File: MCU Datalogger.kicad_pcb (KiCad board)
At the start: 2 copper layers, 29 parts, among them J1 Conn_01x04_Pin, J2 Conn_01x04_Pin, J3 Conn_01x09_Pin, J4 Conn_02x03_Odd_Even, U1 24LC1025, U2 24LC1025, U3 DS1337S_, U4 ATMEGA328P-AU, Y1 32.768 KHZ, Y2 16 MHz

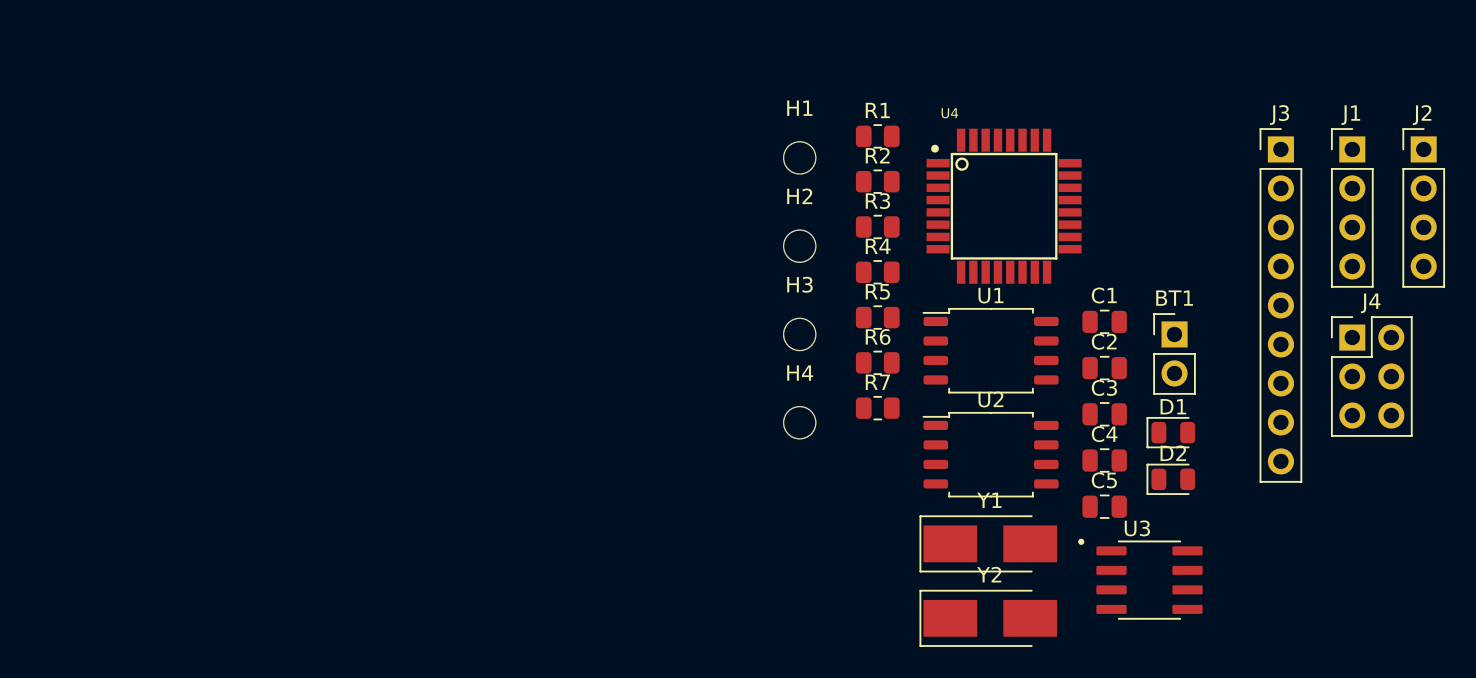
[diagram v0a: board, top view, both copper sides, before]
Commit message: Completed placement of footprints.
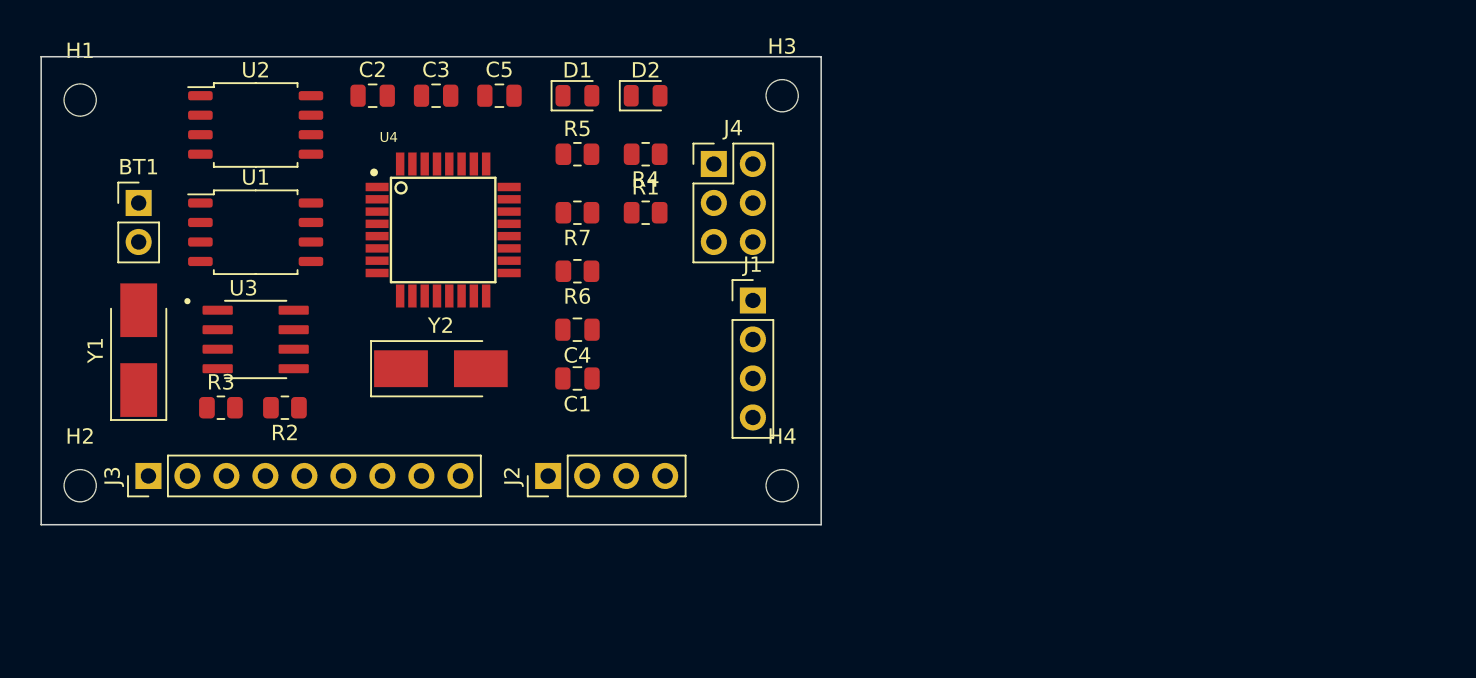
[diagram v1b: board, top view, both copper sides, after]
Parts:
- moved J3 76.8 mm to (83.2, 103.5), turned to 90 degrees
- moved BT1 68.0 mm to (82.5, 85.7)
- moved J2 60.9 mm to (109.2, 103.5), turned to 90 degrees
- moved U3 60.3 mm to (90.2, 94.6)
- moved Y1 56.9 mm to (82.5, 95.3), turned to 90 degrees
- moved U2 52.5 mm to (90.2, 80.6)
- moved C2 50.9 mm to (97.8, 78.7)
- moved H2 49.4 mm to (78.7, 104.1)
- moved U1 48.5 mm to (90.2, 87.6)
- moved C3 48.2 mm to (101.9, 78.7)
- moved C5 47.6 mm to (106.0, 78.7)
- moved H1 47.0 mm to (78.7, 79.0)
- moved D1 44.6 mm to (111.1, 78.7)
- moved R3 44.4 mm to (87.9, 99.1)
- moved J4 43.1 mm to (120.0, 83.2)
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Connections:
- Y1 pad 1: Net-(U3-X1) -> Net-(U3-X2)
- Y1 pad 2: Net-(U3-X2) -> Net-(U3-X1)
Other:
- board outline added: 50.8 x 30.5 mm

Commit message: Routing without GND VCC completed.
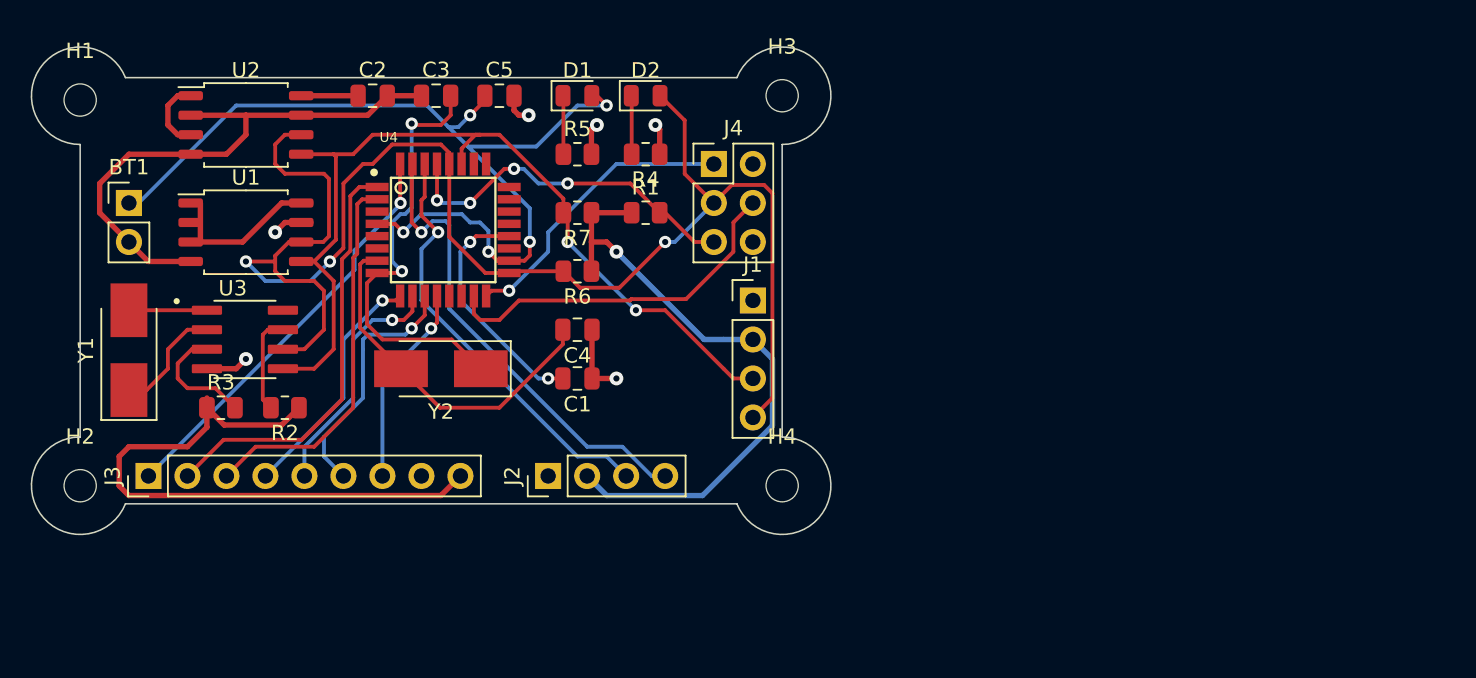
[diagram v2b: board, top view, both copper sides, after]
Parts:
- moved U3 0.70 mm to (89.5, 94.6)
- moved U1 0.64 mm to (89.5, 87.6)
- moved U2 0.64 mm to (89.5, 80.6)
- moved BT1 0.63 mm to (81.9, 85.7)
- moved Y1 0.63 mm to (81.9, 95.3)
- turned Y2 to 180 degrees
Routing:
- net /SCK: track 0.00 -> 102.3 mm, vias 0 -> 3
- net /Vcc: track 0.00 -> 101.9 mm, vias 0 -> 1
- net Net-(BT1-+): track 0.00 -> 61.5 mm, vias 0 -> 5
- net /SDA: track 0.00 -> 56.9 mm, vias 0 -> 2
- net GND: track 0.00 -> 52.4 mm, vias 0 -> 6
- net /TX: track 0.00 -> 31.0 mm, vias 0 -> 1
- net Net-(U4-PB7): track 0.00 -> 28.6 mm, vias 0 -> 2
- net /RX: track 0.00 -> 28.0 mm, vias 0 -> 1
- net /D3: track 0.00 -> 27.6 mm
- net /D2: track 0.00 -> 27.1 mm, vias 0 -> 1
- net /D4: track 0.00 -> 24.9 mm
- net /MOSI: track 0.00 -> 23.8 mm
- net Net-(U4-PB6): track 0.00 -> 23.4 mm
- net /RESET: track 0.00 -> 23.4 mm, vias 0 -> 4
- net /MISO: track 0.00 -> 19.1 mm, vias 0 -> 1
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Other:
- board size 50.8 x 30.5 mm -> 52.1 x 31.7 mm

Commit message: Completed routing.
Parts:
- moved H1 0.28 mm to (78.7, 78.7)
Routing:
- net GND: track 52.4 -> 78.7 mm, vias 6 -> 12
- net /Vcc: track 101.9 -> 117.4 mm, vias 1 -> 3
- net /D4: track 24.9 -> 29.6 mm, vias 0 -> 2
- net /D3: track 27.6 -> 30.5 mm, vias 0 -> 2
- net /D2: track 27.1 -> 30.0 mm
- added copper zone on F.Cu, net /Vcc
- added copper zone on B.Cu, net GND

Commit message: Refined routing complete.
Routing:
- net /D4: track 29.6 -> 26.7 mm
- net /D7: track 16.4 -> 13.9 mm
- net /SCK: track 102.4 -> 100.8 mm
- net /RX: track 28.0 -> 26.5 mm
- net /D2: track 30.0 -> 31.2 mm
- net Net-(U4-AREF): track 15.5 -> 14.7 mm

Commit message: Fixed outstanding issues.
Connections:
- BT1 pad 1: Net-(BT1-+) -> /Vcc
- C5 pad 1: Net-(BT1-+) -> /Vcc
- D1 pad 2: Net-(BT1-+) -> /Vcc
- U4 pad 18: Net-(BT1-+) -> /Vcc
- U4 pad 4: Net-(BT1-+) -> /Vcc
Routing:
- net /Vcc: track 117.4 -> 186.0 mm, vias 3 -> 8
- net Net-(BT1-+): track 61.3 -> 0.00 mm, vias 5 -> 0
- net GND: track 78.7 -> 83.9 mm, vias 12 -> 13
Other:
- board text added: "- 2Mbit EEPROM - RTC - I2C, SPI, GPIOs"
- board text added: "2"
- board text added: "3"
- board text added: "4"
- board text added: "5"
- board text added: "6"
- board text added: "7"
- board text added: "8"
- board text added: "Data logger with the ATMega328P"
- board text added: "GND"
- board text added: "GPIO"
- board text added: "I2C"
- board text added: "ICSP"
- board text added: "ICSP MISO | VCC SCK | MOSI RESET| GND"
- board text added: "RX"
- board text added: "SCK"
- board text added: "SDA"
- board text added: "SERIAL"
- board text added: "TX"
- board text added: "VCC"
